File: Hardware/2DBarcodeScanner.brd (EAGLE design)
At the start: 43.2 x 35.6 mm, 53 parts, among them J1 BARCODE_ENGINE_CONN, Q1 600mA/40V, Q2 600mA/40V, U1 3.3V, U5 CH340C

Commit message: Version x02
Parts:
- removed C5: 0.1uF, SparkFun-Capacitors:0603
- removed C9: 10nF, SparkFun-Capacitors:0603
- removed H1, H4: STAND-OFF, SparkFun-Hardware:STAND-OFF
- removed J3: (no value), SparkFun-Connectors:1X05_NO_SILK
- removed R12: 1k, SparkFun-Resistors:0603
- removed R4: 5.1k, SparkFun-Resistors:0603
- removed U$16: (no value), buzzard_labels:HID5
- removed U$19: (no value), buzzard_labels:SERIAL6
- removed U5: CH340C, SparkFun-IC-Comms:SO016
- added JP1: JUMPER-SMT_2_NC_TRACE_SILK, SparkFun-Jumpers:SMT-JUMPER_2_NC_TRACE_SILK
- J4: device SparkFun-Connectors:USB-C-16P -> SparkFun-Connectors:1X06_NO_SILK
- R1: value 5.1k -> 470
- U$10: device buzzard_labels:SERIAL6 -> buzzard_labels (32):TX__2
- U$11: device Labels:3V3-04 -> buzzard_labels (32):TX__2
- U$12: device buzzard_labels:RX0 -> buzzard_labels (32):RX__1
- U$13: device buzzard_labels:TX1 -> buzzard_labels (32):RX__1
- U$14: device Labels:GND-04 -> buzzard_labels (32):GND__0
- U$15: device buzzard_labels (2):TRIG2 -> buzzard_labels (32):GND__0
- U$2: device Labels:GND-04 -> buzzard_labels:STATUS3
- U$3: device Labels:3V3-04 -> buzzard_labels (32):STAT__5
- U$4: device buzzard_labels:RX0 -> buzzard_labels (32):TRIG__4
- U$5: device buzzard_labels:TX1 -> buzzard_labels (32):TRIG__4
- U$6: device buzzard_labels (2):TRIG2 -> buzzard_labels (32):3V3__3
- U$8: device buzzard_labels:STATUS3 -> buzzard_labels (33):LED0
- U$9: device buzzard_labels:HID5 -> buzzard_labels (32):3V3__3
- moved LS1 28.8 mm to (37.8, 6.35)
- moved U$21 26.8 mm to (9.78, 16.4), turned to 270 degrees
- moved U$9 21.4 mm to (14.0, 6.22), turned to 270 degrees
- moved C3 18.4 mm to (25.0, 20.6), turned to 180 degrees
- moved R3 16.1 mm to (9.40, 14.0)
- moved J4 15.5 mm to (19.1, 1.27), turned to 180 degrees
- moved R1 14.3 mm to (22.6, 1.27), turned to 0 degrees
- moved J1 14.2 mm to (23.2, 16.5)
- moved J2 14.0 mm to (6.35, 11.4)
- moved R10 13.0 mm to (28.8, 21.5), turned to 180 degrees
- moved U$3 12.7 mm to (19.1, 6.86), flipped to the bottom, turned to 270 degrees
- moved H3 12.7 mm to (2.54, 20.3)
- moved U$15 12.5 mm to (6.35, 6.35), flipped to the top, turned to 270 degrees
- moved Q2 12.0 mm to (30.5, 19.1), turned to 270 degrees
- moved R11 11.8 mm to (27.9, 19.1), turned to 90 degrees
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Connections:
- removed net CC1: J4.A5, R4.2
- removed net CC2: J4.B5, R1.2
- removed net D+: J4.A6, J4.B6, U5.5
- removed net D-: J4.A7, J4.B7, U5.6
- removed net N$1: C9.1, U5.4
- removed net N$6: D2.A, R12.1
- new net N$8: D2.A, JP1.1
- new net STATUS_OUT: J4.1, JP1.2, R1.1
- net 3.3V: now also J4.3; no longer J3.5, U5.16
- net 5V: no longer C5.1, J4.VBUS1, J4.VBUS2
- net GND: now also J4.6; no longer C5.2, C9.2, J3.2, J4.GND, J4.GND2, R1.1, R4.1, U5.1
- net N$4: now also R1.2; no longer R12.2
- net RXI: now also J4.5; no longer J3.3, U5.3
- net SCAN_TRIGGER: now also J4.2; no longer J3.1
- net SHLD: no longer J4.SHLD1, J4.SHLD2, J4.SHLD3, J4.SHLD4, J4.SHLD5, J4.SHLD6, J4.SHLD7, J4.SHLD8
- net TXO: now also J4.4; no longer J3.4, U5.2
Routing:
- net SCAN_TRIGGER: track 53.1 -> 25.9 mm
- net TXO: track 46.7 -> 20.7 mm, vias 4 -> 0
- net 5V: track 59.7 -> 34.5 mm, vias 2 -> 3
- net 3.3V: track 72.0 -> 48.1 mm, vias 2 -> 3
- net N$3: track 29.9 -> 8.45 mm, vias 2 -> 0
- net USB_N: track 47.7 -> 26.5 mm
- net USB_P: track 47.6 -> 26.6 mm
- net STATUS_LED: track 23.6 -> 4.72 mm, vias 2 -> 0
- net D-: track 18.7 -> 0.00 mm, vias 2 -> 0
- net D+: track 18.6 -> 0.00 mm, vias 2 -> 0
- net RXI: track 39.4 -> 22.2 mm, vias 4 -> 0
- net N$4: track 6.62 -> 21.2 mm
- net STATUS_OUT: track 0.00 -> 9.39 mm
- net N$2: track 24.7 -> 15.9 mm, vias 4 -> 0
- net N$1: track 4.91 -> 0.00 mm
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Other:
- board size 43.2 x 35.6 mm -> 44.5 x 22.9 mm
- board text added: "x02"
- board text removed: "x01"

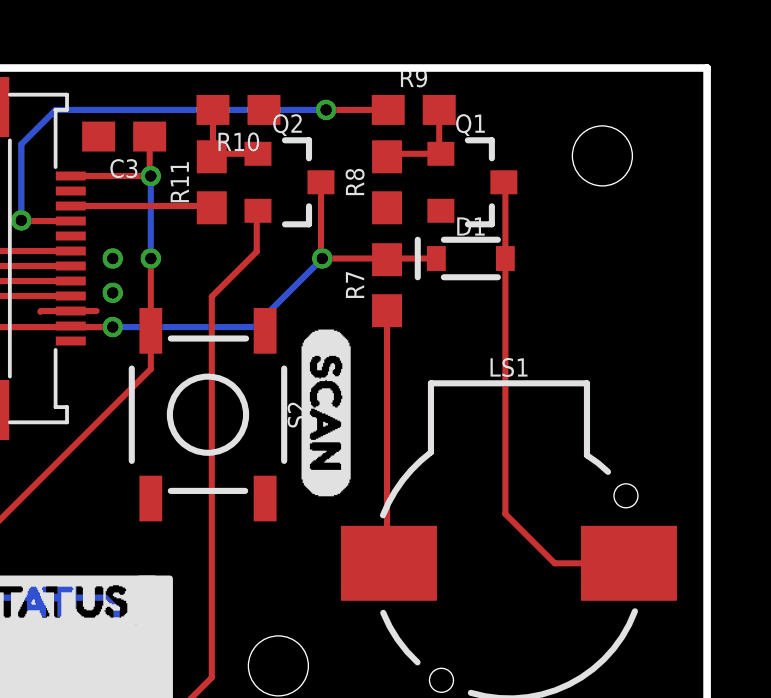
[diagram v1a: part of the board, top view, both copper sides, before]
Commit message: Forgot to pull that stupid diode
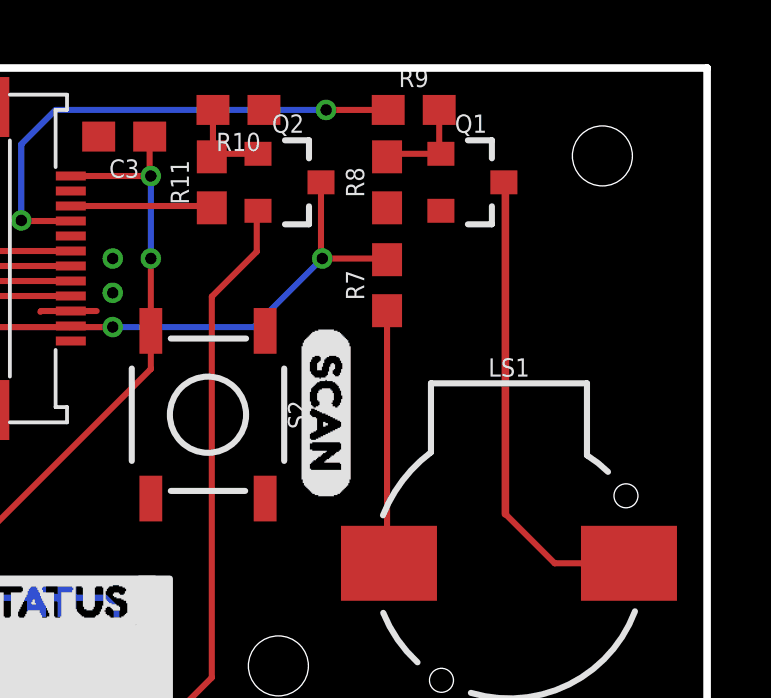
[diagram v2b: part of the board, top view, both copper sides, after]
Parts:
- removed D1: 3.3V, SparkFun-DiscreteSemi:SOD-323
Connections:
- net 3.3V: no longer D1.C
- net N$2: no longer D1.A
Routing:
- net 3.3V: track 48.1 -> 46.5 mm
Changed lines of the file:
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@@
 <attribute name="VALUE" x="37.846" y="12.065" size="0.6096" layer="27" font="vector" ratio="20" align="top-center"/>
-</element>
-<element name="D1" library="SparkFun-DiscreteSemi" package="SOD-323" value="3.3V" x="36.576" y="16.51" smashed="yes">
-<attribute name="NAME" x="36.576" y="17.272" size="0.6096" layer="25" font="vector" ratio="20" align="bottom-center"/>
-<attribute name="PROD_ID" value="DIO-11284" x="36.576" y="16.51" size="1.778" layer="27" font="vector" ratio="15" display="off"/>
-<attribute name="VALUE" x="36.576" y="15.748" size="0.6096" layer="27" font="vector" ratio="20" align="top-center"/>
 </element>
 <element name="R7" library="SparkFun-Resistors" package="0603" value="10" x="33.782" y="15.621" smashed="yes" rot="R90">
@@
 <contactref element="C2" pad="1"/>
 <contactref element="J1" pad="P$11"/>
-<contactref element="D1" pad="C"/>
 <contactref element="R7" pad="2"/>
 <contactref element="Q2" pad="3"/>
@@
 <wire x1="31.58" y1="16.553" x2="31.623" y2="16.51" width="0.2032" layer="1"/>
 <wire x1="33.782" y1="16.471" x2="33.821" y2="16.51" width="0.2032" layer="1"/>
-<wire x1="33.821" y1="16.51" x2="35.426" y2="16.51" width="0.2032" layer="1"/>
 <wire x1="24.638" y1="14.224" x2="29.337" y2="14.224" width="0.2032" layer="16"/>
 <wire x1="29.337" y1="14.224" x2="31.623" y2="16.51" width="0.2032" layer="16"/>
@@
 <contactref element="Q1" pad="3"/>
 <contactref element="LS1" pad="-"/>
-<contactref element="D1" pad="A"/>
 <wire x1="37.676" y1="19.05" x2="37.726" y2="19" width="0.1778" layer="1"/>
-<wire x1="37.726" y1="19" x2="37.726" y2="16.51" width="0.2032" layer="1"/>
-<wire x1="37.726" y1="16.51" x2="37.726" y2="7.994" width="0.2032" layer="1"/>
 <wire x1="37.726" y1="7.994" x2="39.37" y2="6.35" width="0.2032" layer="1"/>
 <wire x1="39.37" y1="6.35" x2="41.846" y2="6.35" width="0.2032" layer="1"/>
+<wire x1="37.726" y1="19" x2="37.726" y2="7.994" width="0.254" layer="1"/>
 </signal>
 <signal name="N$3">
